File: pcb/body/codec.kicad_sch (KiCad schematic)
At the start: 16 parts, among them J5 Headphones, U3 AP7313-18SAG, U4 SGTL5000XNLA3

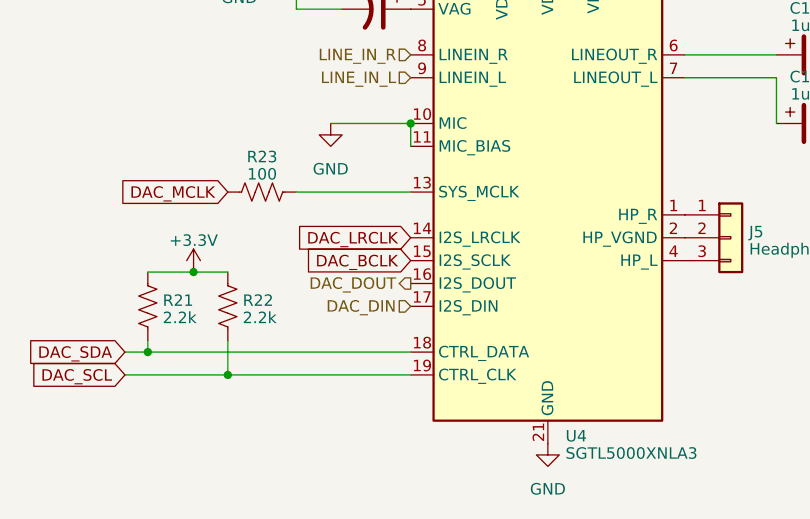
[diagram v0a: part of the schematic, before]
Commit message: linked input stages to codecs
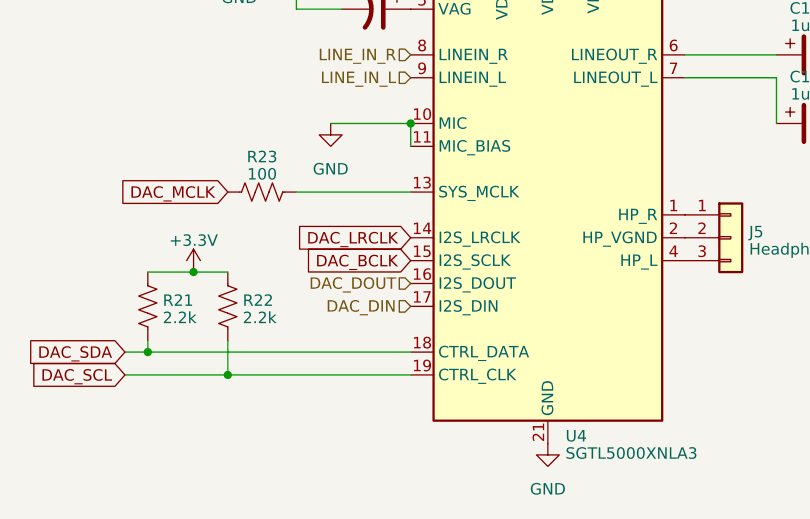
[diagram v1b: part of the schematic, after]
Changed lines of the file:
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@@
     (effects (font (size 1.27 1.27)) (justify left))
   )
-  (hierarchical_label "DAC_DOUT" (shape output) (at 134.62 110.49 180) (fields_autoplaced)
+  (hierarchical_label "DAC_DOUT" (shape input) (at 134.62 110.49 180) (fields_autoplaced)
     (effects (font (size 1.27 1.27)) (justify right))
   )

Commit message: nice progress
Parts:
- removed J5: Headphones, Connector_PinHeader_2.54mm:PinHeader_1x03_P2.54mm_Vertical, symbol Connector_Generic:Conn_01x03
- removed U3: AP7313-18SAG, Package_TO_SOT_SMD:SOT-23, symbol Regulator_Linear:SPX2920M3-3.3_SOT223
- renumbered C10 to C19, C11 to C20, C12 to C21, C14 to C22, C15 to C23, C16 to C24, C17 to C25, C18 to C26, C19 to C27, R21 to R49, R22 to R50, R23 to R51, U4 to U6
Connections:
- net HEADPHONES_L: now reaches U6.1 (HP_R)
- net HEADPHONES_GND: now reaches U6.2 (HP_VGND)
- net HEADPHONES_R: now reaches U6.4 (HP_L)
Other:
- moved on the sheet: C19, C20, C21
